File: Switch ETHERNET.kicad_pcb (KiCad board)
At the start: 4 copper layers, 100 x 72.2 mm, 133 parts, among them J1 Conn_01x04, J2 RJ45_LED, J3 RJ45_LED, J4 RJ45_LED, J5 RJ45_LED, J6 RJ45_LED, J7 Jack-DC, J8 Conn_01x04, J9 Conn_01x02_Pin, Q1 SI2301-ZE, SW1 SW_Push, U1 RTL8367N-VB-CG, U2 TPS563201, U3 TPS563201, Y1 25MHz

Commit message: IC re-positioned
Made the IC in 45 degree and increased the spaces between the High-speed traces to avoid dross talks
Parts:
- moved C54 161.5 mm to (145.5, 72.5)
- moved C55 161.5 mm to (145.5, 74.4)
- moved C53 59.9 mm to (243.6, 80.1)
- moved C40 51.3 mm to (238.8, 92.9)
- moved C44 51.3 mm to (236.6, 92.9)
- moved C50 51.3 mm to (232.8, 85.5)
- moved C39 51.3 mm to (238.2, 85.0)
- moved C41 51.3 mm to (230.0, 91.9)
- moved C42 51.3 mm to (240.8, 85.6)
- moved C43 51.3 mm to (240.9, 91.4)
- moved C45 51.3 mm to (230.0, 92.9)
- moved C46 51.3 mm to (235.0, 85.0)
- moved C47 51.3 mm to (240.9, 87.6)
- moved C48 51.3 mm to (240.6, 92.9)
- moved C49 51.3 mm to (240.9, 89.5)
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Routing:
- net P4MDID_N: track 33.0 -> 54.2 mm
- net P4MDID_P: track 33.0 -> 54.1 mm
- net P4MDIC_N: track 29.1 -> 46.7 mm
- net P4MDIC_P: track 29.1 -> 46.7 mm
- net P4MDIB_N: track 24.7 -> 39.3 mm
- net P4MDIB_P: track 24.6 -> 39.2 mm
- net P0MDIB_P: track 60.6 -> 47.9 mm
- net P4MDIA_P: track 20.0 -> 32.7 mm
- net P4MDIA_N: track 20.0 -> 32.6 mm
- net P0MDIB_N: track 60.2 -> 47.8 mm
- net P0MDIA_N: track 65.8 -> 53.9 mm
- net P0MDIA_P: track 65.8 -> 53.9 mm
- net P3MDID_P: track 13.4 -> 24.6 mm
- net P0MDID_N: track 49.8 -> 38.7 mm
- net P0MDID_P: track 49.8 -> 38.7 mm
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
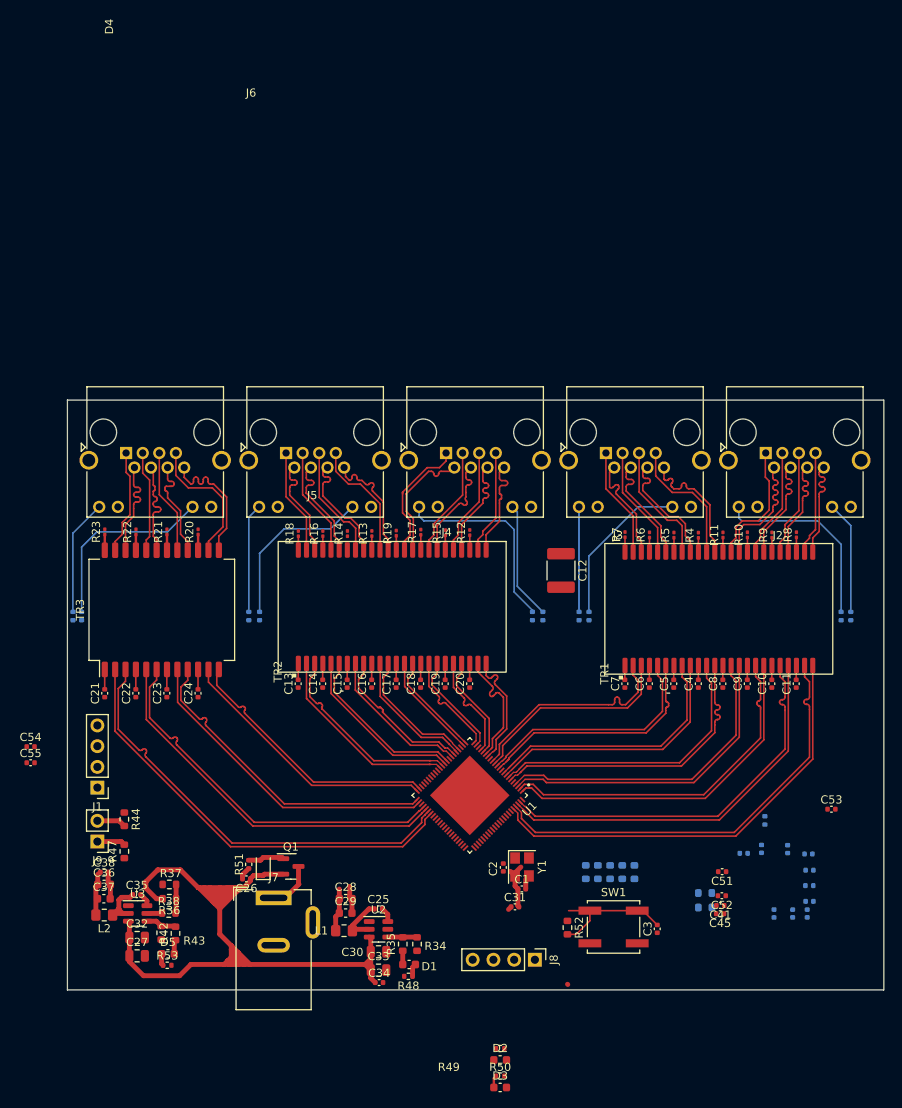
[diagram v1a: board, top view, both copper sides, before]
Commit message: Buck converters and power rails routed
I finished routing the two Buck converters and routed the power rails till the IC + placement of decoupling capacitors + in-board spaces between the analog and digital sections + routed the LEDs of the RJ-45 connectors
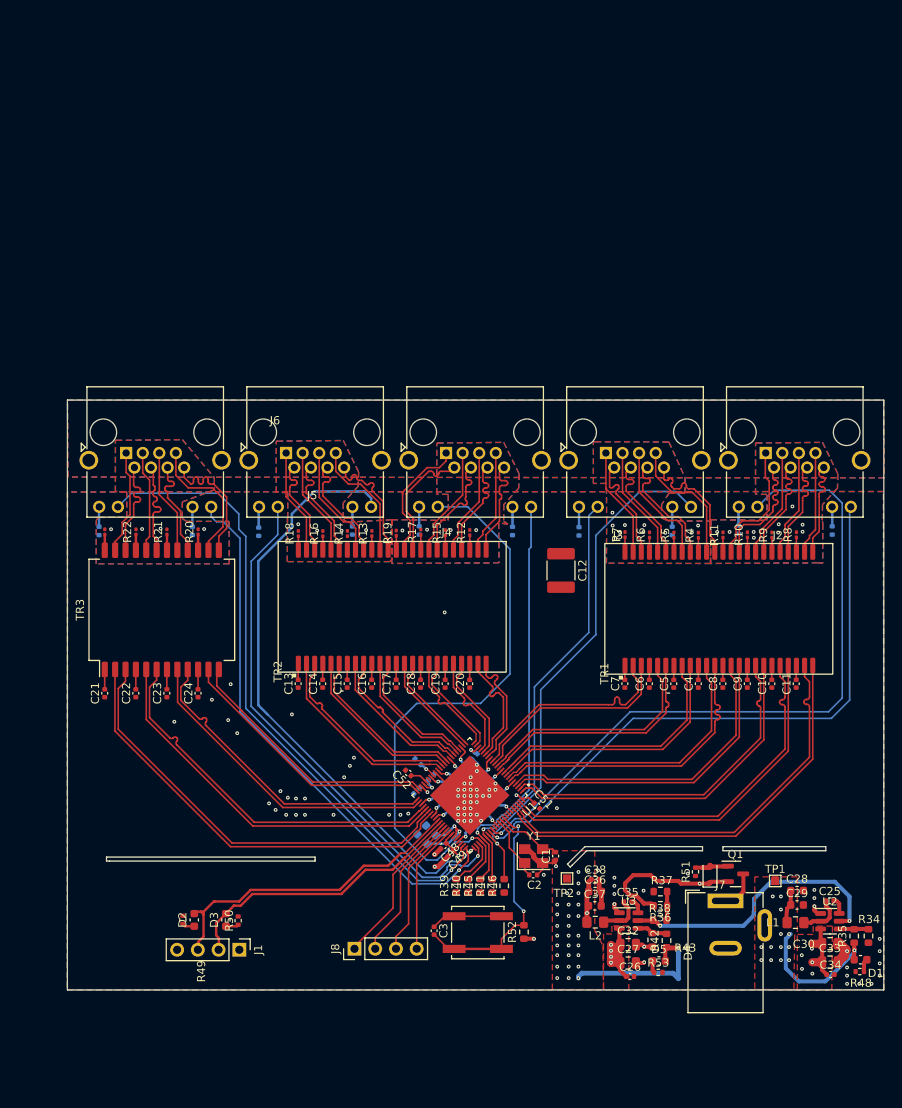
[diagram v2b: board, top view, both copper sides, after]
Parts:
- removed J9: Conn_01x02_Pin, Connector_PinHeader_2.54mm:PinHeader_1x02_P2.54mm_Vertical
- removed R44, R47: 4.7K, Resistor_SMD:R_0603_1608Metric
- added C56: 100nF, Capacitor_SMD:C_0402_1005Metric, B.Cu at (198.3, 75.8)
- added C57: 100nF, Capacitor_SMD:C_0402_1005Metric, B.Cu at (194.5, 76.2)
- added TP1: 3.3V, TestPoint:TestPoint_Pad_1.0x1.0mm, F.Cu at (236.7, 88.9)
- added TP2: 1.1V, TestPoint:TestPoint_Pad_1.0x1.0mm, F.Cu at (211.2, 88.6)
- C31, C41, C45, C53, C54, C55: moved to B.Cu
- C48, C49, R39, R40, R41, R45, R46: moved to F.Cu
- moved C27 60.2 mm to (218.7, 99.0)
- moved C32 60.2 mm to (218.7, 96.7)
- moved C37 60.2 mm to (214.6, 92.0)
- moved C38 60.2 mm to (214.7, 88.7)
- moved D5 60.2 mm to (222.5, 98.7)
- moved L2 60.2 mm to (214.7, 94.0)
- moved R38 60.2 mm to (222.6, 93.7)
- moved R53 60.2 mm to (222.4, 100.1)
- moved U3 60.2 mm to (218.7, 93.8)
- moved C35 60.2 mm to (218.6, 91.5)
- moved C36 60.2 mm to (214.6, 90.2)
- moved R36 60.2 mm to (222.6, 92.0)
- moved R37 60.2 mm to (222.6, 90.2)
- moved R42 60.2 mm to (223.4, 96.2)
- moved R43 60.2 mm to (221.6, 96.1)
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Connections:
- C28 pad 1: +1V1 -> +3.3V
- C29 pad 1: +1V1 -> +3.3V
- C31 pad 1: +1V1 -> +3.3V
- C39 pad 1: +1V1 -> +3.3V
- C40 pad 1: +1V1 -> +3.3V
- C41 pad 1: +1V1 -> +3.3V
- C42 pad 1: +1V1 -> +3.3V
- C44 pad 1: +1V1 -> +3.3V
- C52 pad 1: +1V1 -> +3.3V
- C54 pad 1: +1V1 -> +3.3V
- C55 pad 1: +1V1 -> +3.3V
- D1 pad 2: +1V1 -> +3.3V
- J1 pad 1: +1V1 -> +3.3V
- L1 pad 2: +1V1 -> +3.3V
- R35 pad 1: +1V1 -> +3.3V
- R52 pad 1: +1V1 -> +3.3V
- U1 pad 25: +1V1 -> +3.3V
- U1 pad 35: +1V1 -> +3.3V
- U1 pad 40: +1V1 -> +3.3V
- U1 pad 42: +1V1 -> +3.3V
- U1 pad 5: +1V1 -> +3.3V
- U1 pad 52: +1V1 -> +3.3V
- U1 pad 63: +1V1 -> +3.3V
- U1 pad 77: +1V1 -> +3.3V
- U1 pad 81: SCK -> unconnected-(U1-SCK/MMD_MDC/EN_EEE-Pad81)
- U1 pad 82: SDA -> unconnected-(U1-SDA-Pad82)
- U1 pad 83: +1V1 -> +3.3V
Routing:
- net +3.3V: track 0.00 -> 223.0 mm, vias 0 -> 23
- net +1V1: track 14.6 -> 116.2 mm, vias 0 -> 41
- net P0LED0: track 0.00 -> 85.7 mm, vias 0 -> 1
- net P4LED0: track 0.00 -> 79.0 mm, vias 0 -> 1
- net P0LED1: track 0.00 -> 75.3 mm, vias 0 -> 1
- net P2LED0: track 0.00 -> 74.8 mm, vias 0 -> 1
- net P3LED1: track 0.00 -> 73.7 mm, vias 0 -> 1
- net P4LED1: track 0.00 -> 66.6 mm, vias 0 -> 1
- net P3LED0: track 0.00 -> 65.0 mm, vias 0 -> 1
- net P1LED1: track 0.00 -> 64.2 mm, vias 0 -> 1
- net P1LED0: track 0.00 -> 52.7 mm, vias 0 -> 1
- net P2LED1: track 0.00 -> 50.4 mm, vias 0 -> 1
- net GND: track 14.5 -> 58.5 mm, vias 0 -> 81
- net Rx_UART: track 0.00 -> 39.8 mm
- net HV_CHASIS: track 0.00 -> 38.1 mm, vias 0 -> 30
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- added copper zone on F.Cu, net +1V1
- added copper zone on In2.Cu, net +1V1
- added copper zone on F.Cu, net +3.3V
- added copper zone on In2.Cu, net +3.3V
- added copper zone on B.Cu, net Earth
- added copper zone on F.Cu, net Earth
- added copper zone on In1.Cu, net Earth
- added copper zone on In2.Cu, net Earth
- added copper zone on B.Cu, net GND
- added copper zone on F.Cu, net GND
- added copper zone on B.Cu, net HV_CHASIS
- added copper zone on F.Cu, net HV_CHASIS
- added copper zone on In2.Cu, net HV_CHASIS
- added copper zone on F.Cu, net VCC
- added copper zone on In2.Cu, net VCC
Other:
- outline, holes or cut-outs redrawn

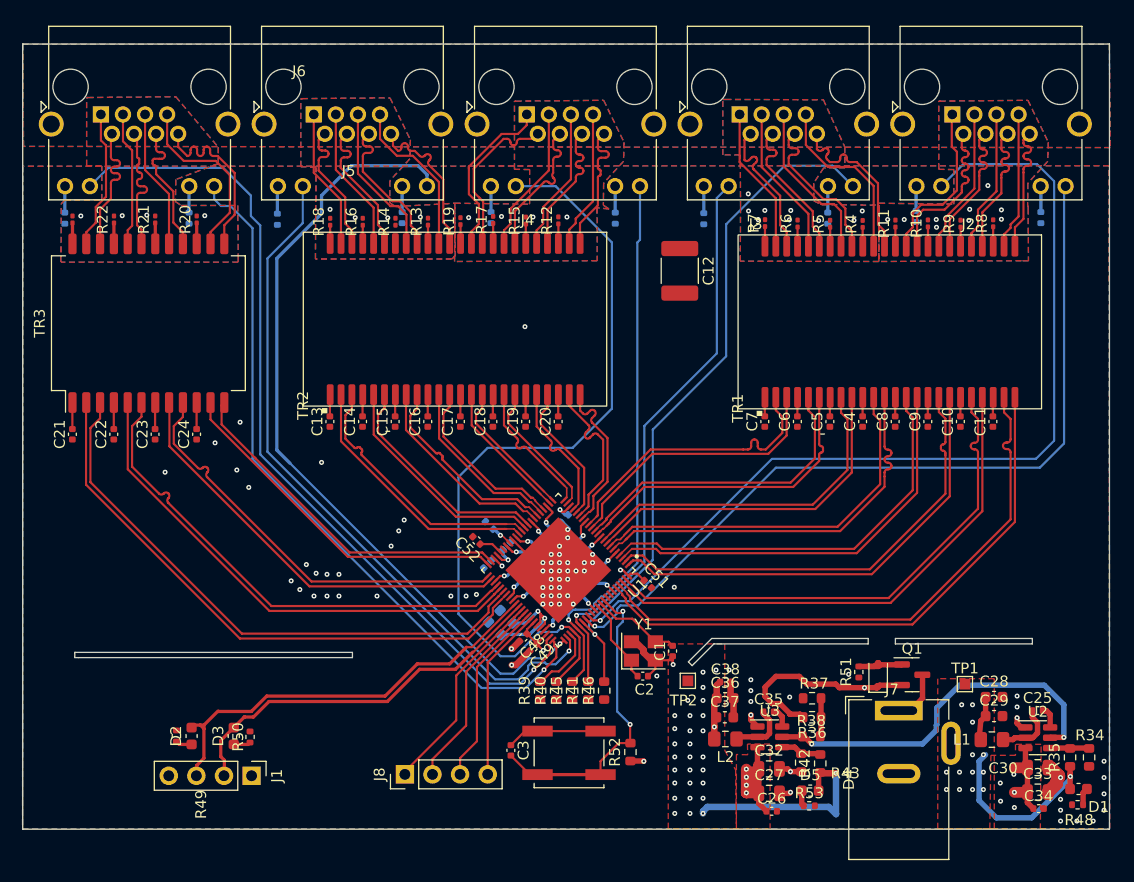
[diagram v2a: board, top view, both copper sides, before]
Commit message: Finished routing and Layout
Finished routing and length matching for the pairs + connecting power planes + reference designators placement
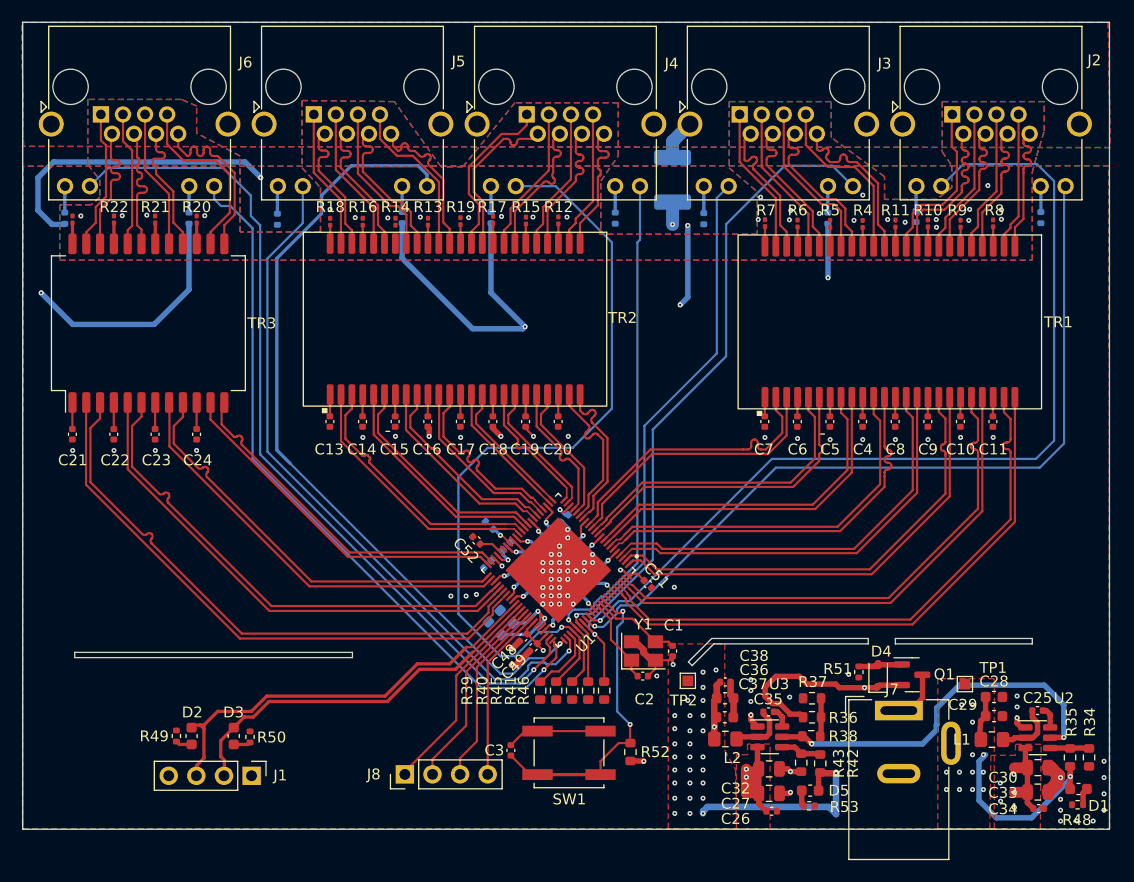
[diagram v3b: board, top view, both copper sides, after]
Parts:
- C12: moved to B.Cu
- moved C12 8.40 mm to (209.8, 42.5)
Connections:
- J2 pad SH: (no net) -> Earth
- J3 pad SH: (no net) -> Earth
- J4 pad SH: (no net) -> Earth
- J5 pad SH: (no net) -> Earth
- J6 pad SH: (no net) -> Earth
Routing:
- net GND: track 58.5 -> 180.7 mm, vias 81 -> 87
- net HV_CHASIS: track 38.1 -> 15.4 mm, vias 30 -> 28
- net Earth: track 0.00 -> 3.74 mm
- net P3MDIA_P: track 16.3 -> 17.9 mm
- net +3.3V: track 223.0 -> 222.0 mm
- net P4MDID_P: track 53.4 -> 54.1 mm
- net VCC: vias 10 -> 8
- net +1V1: vias 41 -> 40
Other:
- board size 100 x 72.2 mm -> 100 x 74.2 mm

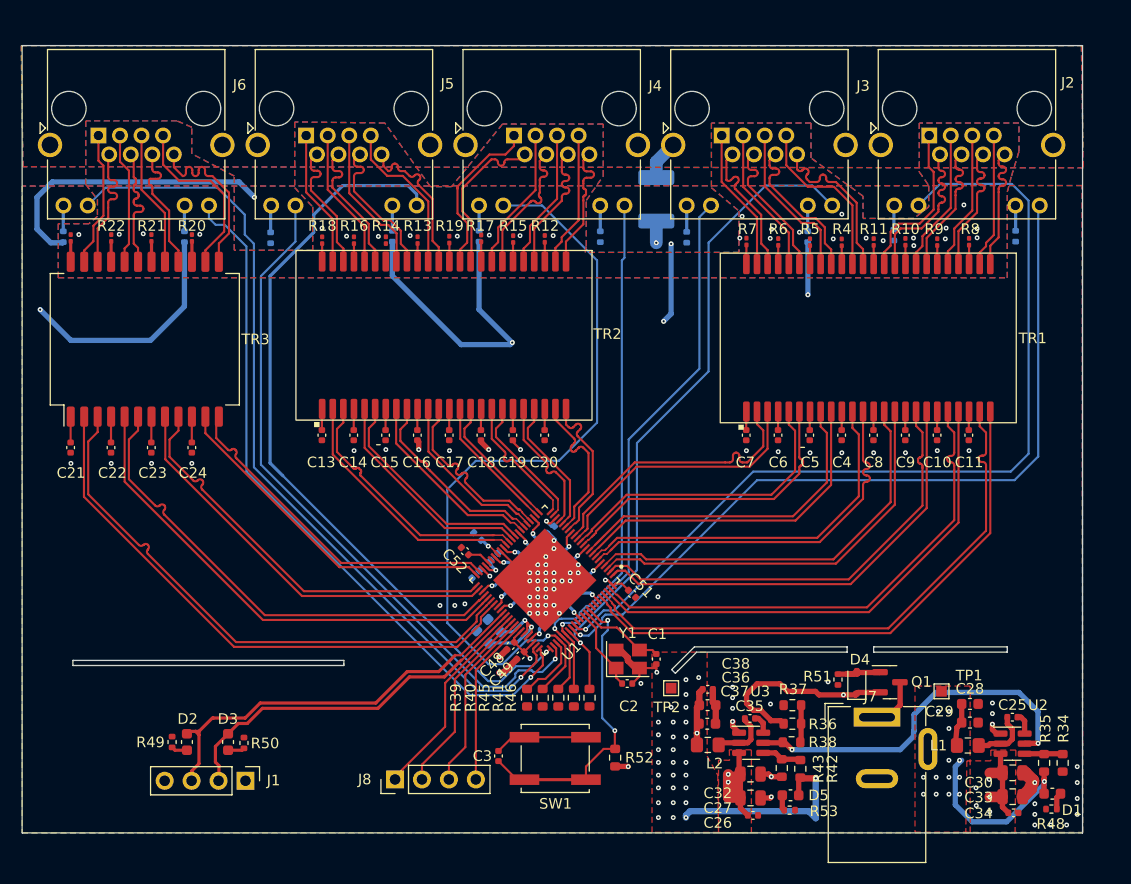
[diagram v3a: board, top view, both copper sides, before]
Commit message: Added Stitching Vias and Texts
Added the texts and finished the overall layout + Added stitching vias to minimize inductance + Exposed board frame as a shield
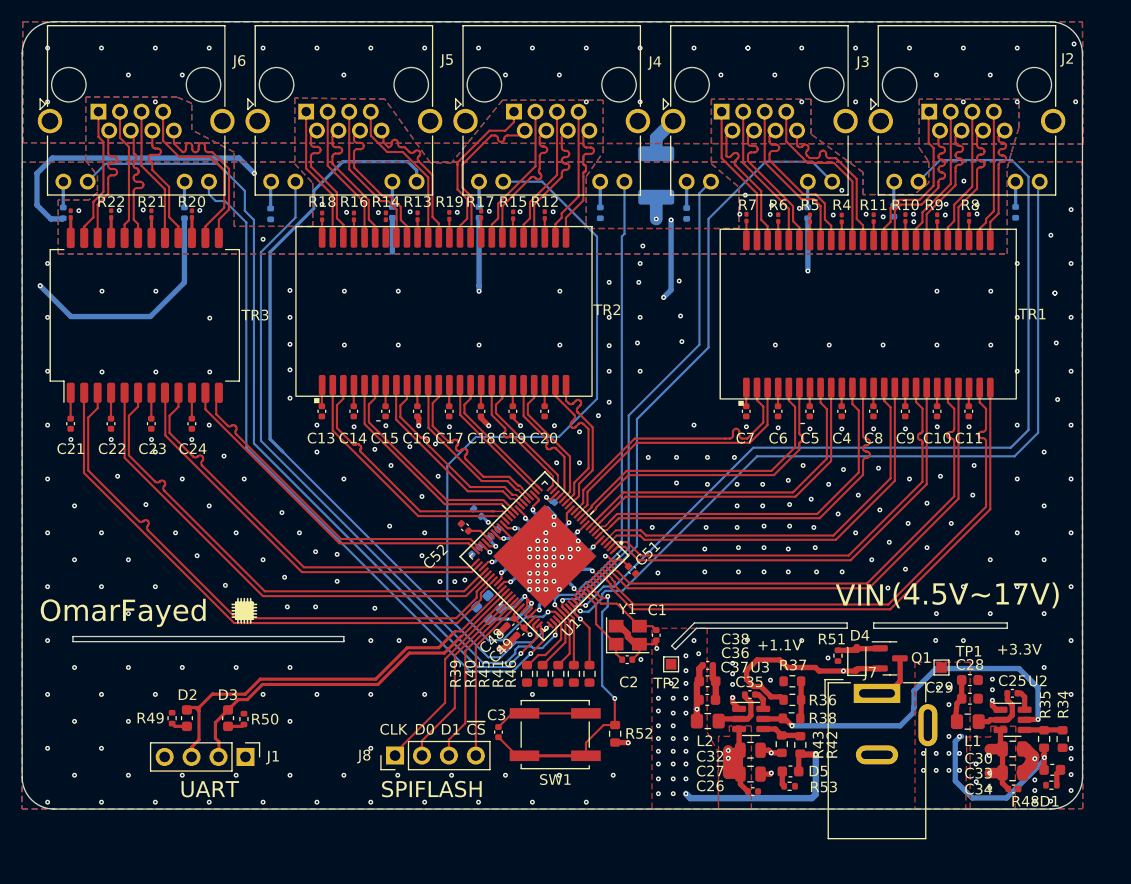
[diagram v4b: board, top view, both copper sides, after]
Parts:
- moved C1 2.25 mm to (209.8, 83.6)
- moved C12 2.25 mm to (209.8, 40.2)
- moved C2 2.25 mm to (207.1, 85.9)
- moved C21 2.25 mm to (154.6, 63.7)
- moved C22 2.25 mm to (158.4, 63.7)
- moved C23 2.25 mm to (162.2, 63.7)
- moved C24 2.25 mm to (166.0, 63.7)
- moved C25 2.25 mm to (243.4, 89.1)
- moved C26 2.25 mm to (218.9, 98.3)
- moved C27 2.25 mm to (218.7, 96.7)
- moved C28 2.25 mm to (239.4, 87.8)
- moved C29 2.25 mm to (239.4, 89.6)
- moved C3 2.25 mm to (194.9, 92.7)
- moved C30 2.25 mm to (243.4, 94.3)
- moved C31 2.25 mm to (201.0, 78.0)
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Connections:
- J7 pad 3: (no net) -> GND
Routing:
- net +3.3V: track 222.0 -> 96.3 mm
- net GND: track 180.7 -> 159.3 mm, vias 87 -> 307
- net +1V1: track 116.2 -> 114.1 mm, vias 40 -> 41
- net HV_CHASIS: vias 28 -> 34
- net Earth: vias 0 -> 35
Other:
- outline, holes or cut-outs redrawn
- board text added: "(4.5V~17V)"
- board text added: "+1.1V"
- board text added: "+3.3V"
- board text added: "4/6/23"
- board text added: "CLK"
- board text added: "D0"
- board text added: "D1"
- board text added: "OmarFayed"
- board text added: "SPIFLASH"
- board text added: "UART"
- board text added: "VIN"
- board text added: "~{CS}"
